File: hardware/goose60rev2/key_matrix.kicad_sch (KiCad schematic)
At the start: 122 parts, among them SW1_1 SW_Push, SW1_10 SW_Push, SW1_11 SW_Push, SW1_12 SW_Push, SW1_13 SW_Push, SW1_14 SW_Push, SW1_2 SW_Push, SW1_3 SW_Push, SW1_4 SW_Push, SW1_5 SW_Push, SW1_6 SW_Push, SW1_7 SW_Push, SW1_8 SW_Push, SW1_9 SW_Push, SW2_1 SW_Push, SW2_10 SW_Push, SW2_11 SW_Push, SW2_12 SW_Push, SW2_13 SW_Push, SW2_14 SW_Push, SW2_2 SW_Push, SW2_3 SW_Push, SW2_4 SW_Push, SW2_5 SW_Push, SW2_6 SW_Push, SW2_7 SW_Push, SW2_8 SW_Push, SW2_9 SW_Push, SW3_1 SW_Push, SW3_10 SW_Push, SW3_11 SW_Push, SW3_12 SW_Push, SW3_14 SW_Push, SW3_2 SW_Push, SW3_3 SW_Push, SW3_4 SW_Push, SW3_5 SW_Push, SW3_6 SW_Push, SW3_7 SW_Push, SW3_8 SW_Push, SW3_9 SW_Push, SW4_1 SW_Push, SW4_10 SW_Push, SW4_11 SW_Push, SW4_12 SW_Push, SW4_14 SW_Push, SW4_3 SW_Push, SW4_4 SW_Push, SW4_5 SW_Push, SW4_6 SW_Push, SW4_7 SW_Push, SW4_8 SW_Push, SW4_9 SW_Push, SW5_1 SW_Push, SW5_11 SW_Push, SW5_12 SW_Push, SW5_13 SW_Push, SW5_14 SW_Push, SW5_2 SW_Push, SW5_3 SW_Push, SW5_7 SW_Push

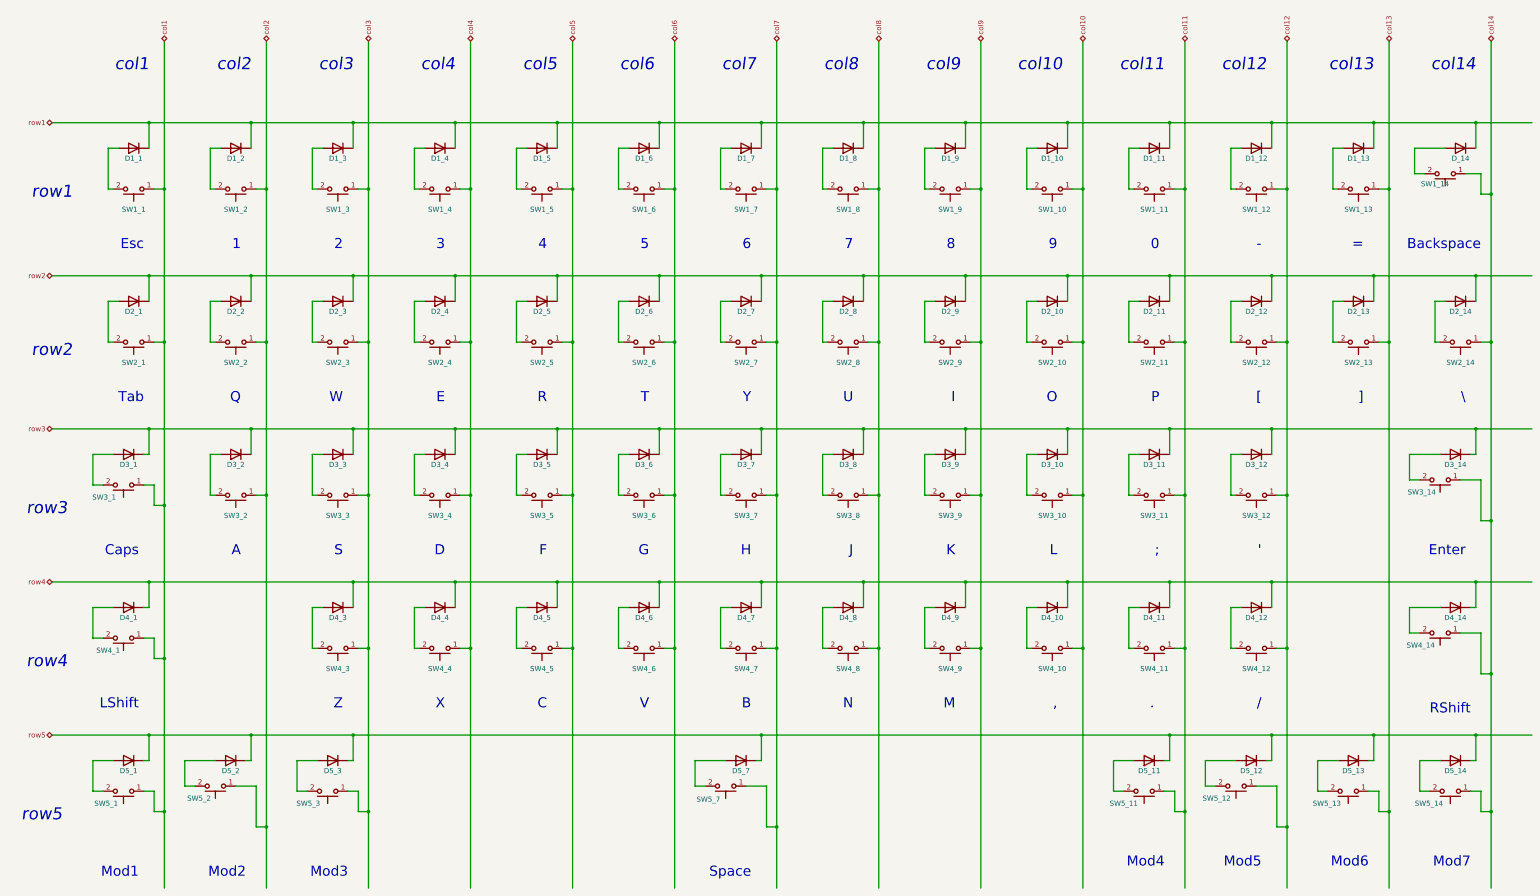
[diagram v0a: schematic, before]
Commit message: [WIP] modify sch design and add new connector
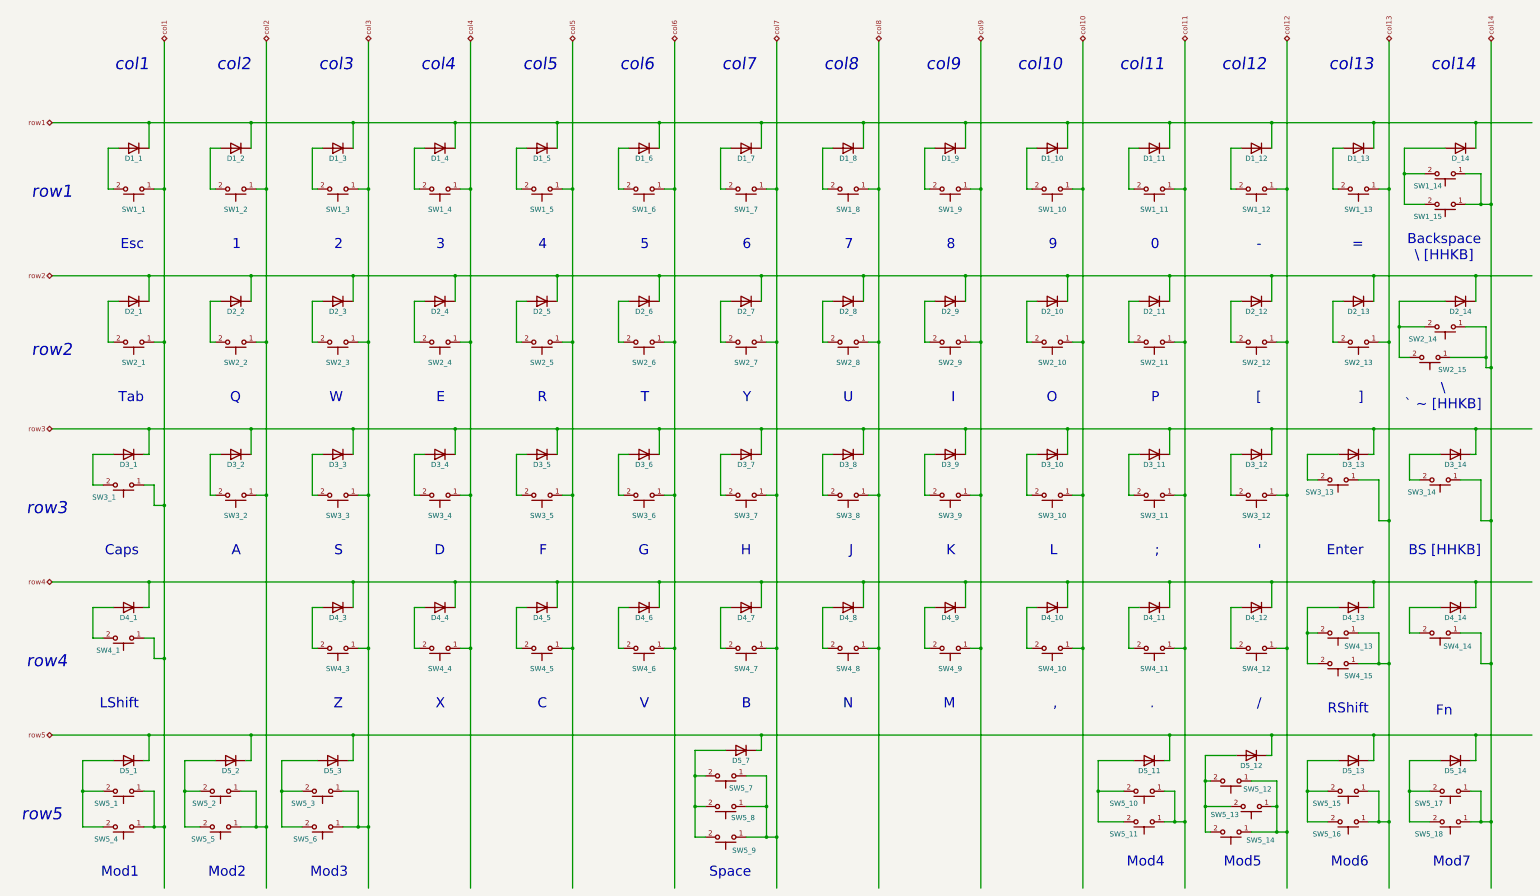
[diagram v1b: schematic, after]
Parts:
- added D3_13, D4_13: 1N4148, Diode_SMD:D_0805_2012Metric, symbol Diode:1N4148
- added SW1_15: SW_Push, Switch_Keyboard_Hotswap_Kailh:SW_Hotswap_Kailh_MX_2.00u, symbol Switch:SW_Push
- added SW2_15: SW_Push, Switch_Keyboard_Hotswap_Kailh:SW_Hotswap_Kailh_MX_1.50u, symbol Switch:SW_Push
- added SW3_13: SW_Push, Switch_Keyboard_Hotswap_Kailh:SW_Hotswap_Kailh_MX_2.25u, symbol Switch:SW_Push
- added SW4_13, SW4_15: SW_Push, Switch_Keyboard_Hotswap_Kailh:SW_Hotswap_Kailh_MX_2.75u, symbol Switch:SW_Push
- added SW5_11, SW5_13, SW5_14, SW5_16, SW5_18, SW5_4, SW5_5, SW5_6: SW_Push, Switch_Keyboard_Hotswap_Kailh:SW_Hotswap_Kailh_MX_1.25u, symbol Switch:SW_Push
- added SW5_8, SW5_9: SW_Push, Switch_Keyboard_Hotswap_Kailh:SW_Hotswap_Kailh_MX_6.25u, symbol Switch:SW_Push
- SW1_1, SW1_10, SW1_11, SW1_12, SW1_13, SW1_2, SW1_3, SW1_4, SW1_5, SW1_6, SW1_7, SW1_8, SW1_9, SW2_10, SW2_11, SW2_12, SW2_13, SW2_2, SW2_3, SW2_4, SW2_5, SW2_6, SW2_7, SW2_8, SW2_9, SW3_10, SW3_11, SW3_12, SW3_2, SW3_3, SW3_4, SW3_5, SW3_6, SW3_7, SW3_8, SW3_9, SW4_10, SW4_11, SW4_12, SW4_3, SW4_4, SW4_5, SW4_6, SW4_7, SW4_8, SW4_9: footprint Keyboard_Hotswap_Kailh:SW_Hotswap_Kailh_MX -> Switch_Keyboard_Hotswap_Kailh:SW_Hotswap_Kailh_MX_1.00u
- SW1_14: footprint Keyboard_Hotswap_Kailh:SW_Hotswap_Kailh_MX -> Switch_Keyboard_Hotswap_Kailh:SW_Hotswap_Kailh_MX_2.00u
- SW2_1, SW2_14: footprint Keyboard_Hotswap_Kailh:SW_Hotswap_Kailh_MX -> Switch_Keyboard_Hotswap_Kailh:SW_Hotswap_Kailh_MX_1.50u
- SW3_1: footprint Keyboard_Hotswap_Kailh:SW_Hotswap_Kailh_MX -> Switch_Keyboard_Hotswap_Kailh:SW_Hotswap_Kailh_MX_1.75u
- SW3_14, SW4_1: footprint Keyboard_Hotswap_Kailh:SW_Hotswap_Kailh_MX -> Switch_Keyboard_Hotswap_Kailh:SW_Hotswap_Kailh_MX_2.25u
- SW4_14: footprint Keyboard_Hotswap_Kailh:SW_Hotswap_Kailh_MX -> Switch_Keyboard_Hotswap_Kailh:SW_Hotswap_Kailh_MX_2.75u
- SW5_1, SW5_12, SW5_2, SW5_3: footprint Keyboard_Hotswap_Kailh:SW_Hotswap_Kailh_MX -> Switch_Keyboard_Hotswap_Kailh:SW_Hotswap_Kailh_MX_1.25u
- SW5_10: renamed from SW5_11; footprint Keyboard_Hotswap_Kailh:SW_Hotswap_Kailh_MX -> Switch_Keyboard_Hotswap_Kailh:SW_Hotswap_Kailh_MX_1.25u
- SW5_15: renamed from SW5_13; footprint Keyboard_Hotswap_Kailh:SW_Hotswap_Kailh_MX -> Switch_Keyboard_Hotswap_Kailh:SW_Hotswap_Kailh_MX_1.25u
- SW5_17: renamed from SW5_14; footprint Keyboard_Hotswap_Kailh:SW_Hotswap_Kailh_MX -> Switch_Keyboard_Hotswap_Kailh:SW_Hotswap_Kailh_MX_1.25u
- SW5_7: footprint Keyboard_Hotswap_Kailh:SW_Hotswap_Kailh_MX -> Switch_Keyboard_Hotswap_Kailh:SW_Hotswap_Kailh_MX_6.25u
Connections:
- net col1: now also SW5_4.1
- net col11: now also SW5_11.1
- net col12: now also SW5_13.1, SW5_14.1
- net col13: now also SW3_13.1, SW4_13.1, SW4_15.1, SW5_16.1
- net col14: now also SW1_15.1, SW2_15.1, SW5_18.1
- net col2: now also SW5_5.1
- net col3: now also SW5_6.1
- net col7: now also SW5_8.1, SW5_9.1
- net row3: now also D3_13.1 (K)
- net row4: now also D4_13.1 (K)
- net at D5_1.2 (A), SW5_1.2: now also SW5_4.2
- net at D5_3.2 (A), SW5_3.2: now also SW5_6.2
- net at D5_12.2 (A), SW5_12.2: now also SW5_13.2, SW5_14.2
- net at D2_14.2 (A), SW2_14.2: now also SW2_15.2
- net at D5_2.2 (A), SW5_2.2: now also SW5_5.2
- net at D_14.2 (A), SW1_14.2: now also SW1_15.2
- net at D5_11.2 (A), SW5_10.2: now also SW5_11.2
- net at D5_14.2 (A), SW5_17.2: now also SW5_18.2
- net at D5_13.2 (A), SW5_15.2: now also SW5_16.2
- net at D5_7.2 (A), SW5_7.2: now also SW5_8.2, SW5_9.2
- new net: D3_13.2 (A), SW3_13.2
- new net: D4_13.2 (A), SW4_13.2, SW4_15.2
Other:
- note added: "BS [HHKB]"
- note added: "Backspace \ [HHKB]"
- note added: "Fn"
- note added: "\ ` ~ [HHKB]"
- note removed: "Backspace"
- note removed: "\"
- moved on the sheet: D5_12, D5_7, SW2_14, SW5_12, SW5_2, SW5_3, SW5_7
